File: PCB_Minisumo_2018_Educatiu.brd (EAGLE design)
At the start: 74.9 x 93 mm, 91 parts, among them Q1 BC817, Q2 BC817, Q3 BC817

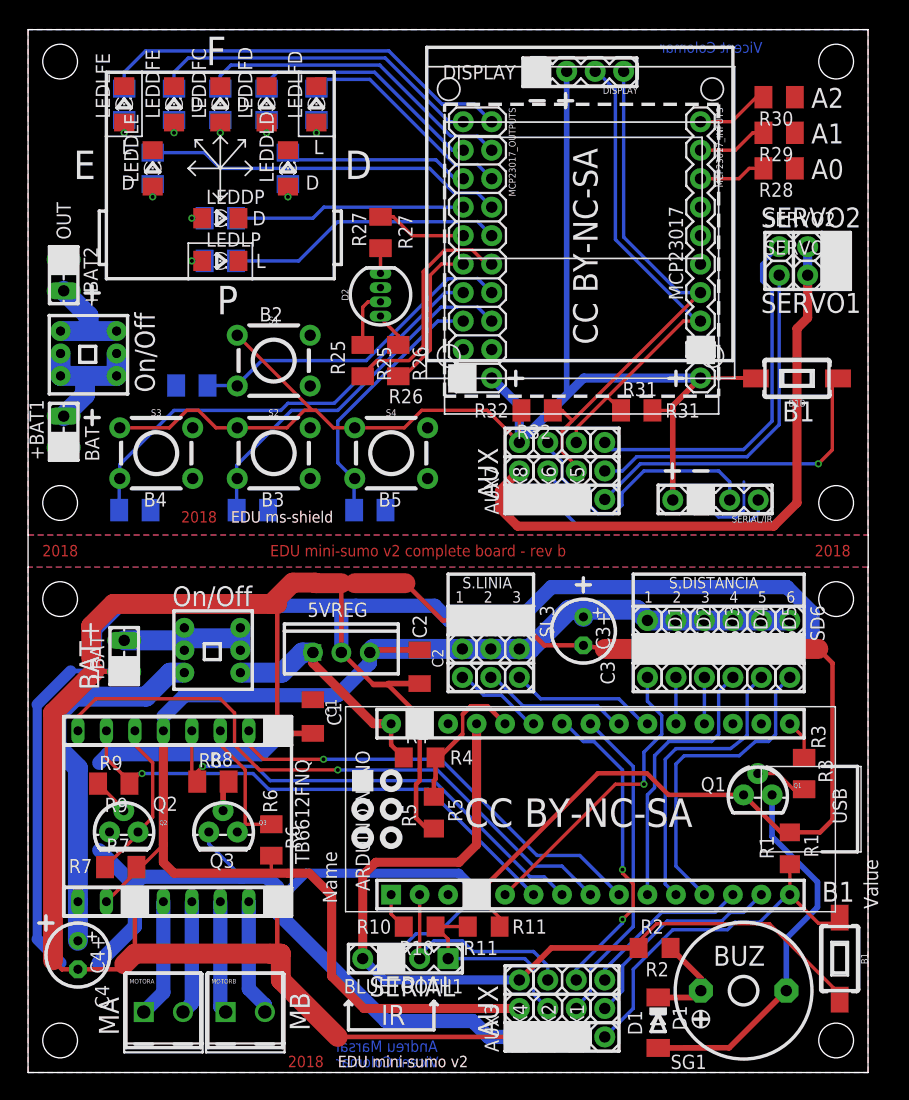
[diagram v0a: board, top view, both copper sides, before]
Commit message: Add files via upload
Corregits petits defectes en la placa.
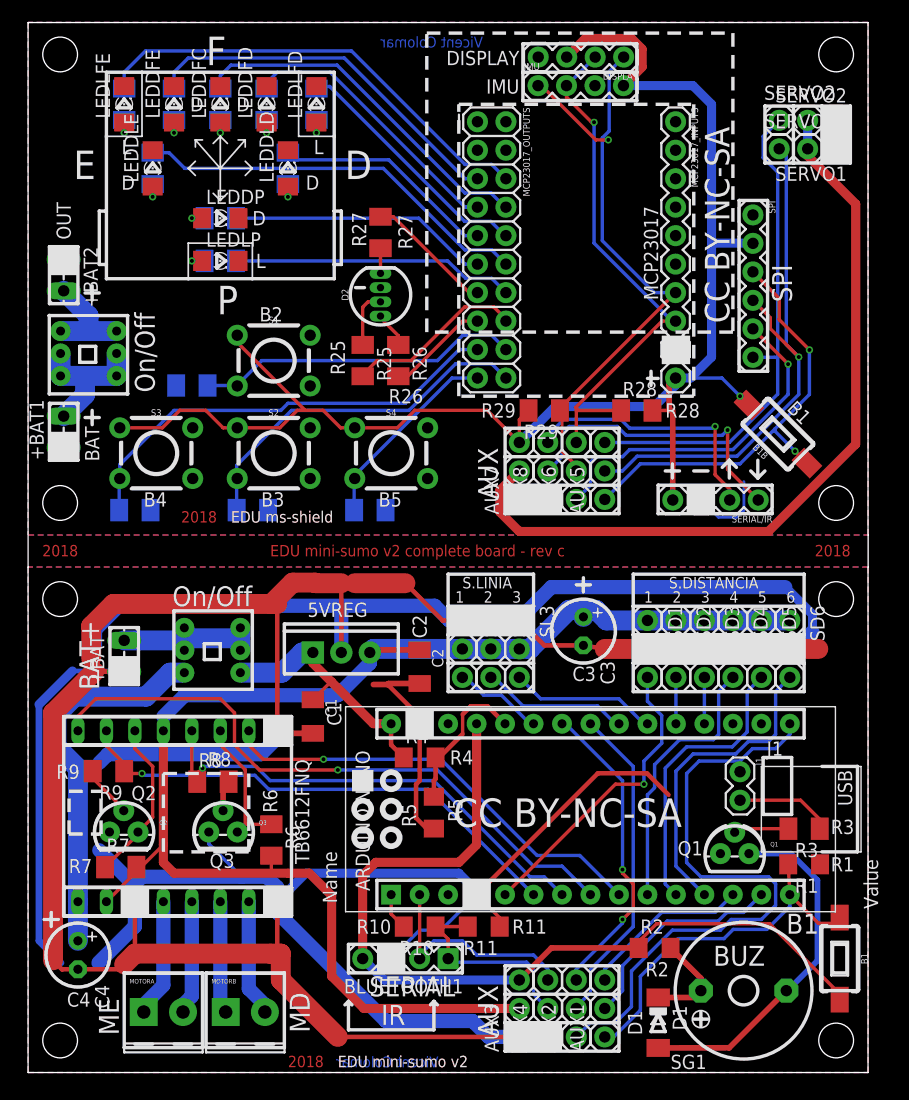
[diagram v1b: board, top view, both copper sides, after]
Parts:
- removed R30: 0R, rcl:M1206
- removed R31, R32: 4K7, rcl:M1206
- added IMU: (no value), SparkFun-Connectors:1X04
- added J1: (no value), SparkFun-Connectors:1X02
- added SPI: (no value), SparkFun-Connectors:1X06
- R28, R29: value 0R -> 4K7
- moved R29 32.4 mm to (46.0, 59.1)
- moved R28 25.0 mm to (54.3, 59.1), turned to 0 degrees
- moved SERVO2 11.3 mm to (67.0, 84.9)
- moved SERVO1 11.3 mm to (67.0, 82.4)
- moved Q1 5.63 mm to (63.0, 19.5)
- moved B1B 5.25 mm to (66.9, 56.9), turned to 135 degrees
- moved R3 4.92 mm to (69.2, 21.7), turned to 180 degrees
- moved MCP23017_INPUTS 2.22 mm to (57.8, 84.8)
- moved R1 1.91 mm to (69.2, 18.6), turned to 180 degrees
- moved DISPLAY 1.27 mm to (53.1, 90.6)
- moved MCP23017_OUTPUTS 1.27 mm to (40.1, 84.8)
- moved R9 1.21 mm to (7.17, 26.9)
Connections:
- removed net BUZZ: R3.1, U$1.D13
- new net N$1: J1.2, R3.1
- new net N$50: MCP23017_OUTPUTS.1
- new net N$51: MCP23017_OUTPUTS.2
- new net SCK_BUZZ: AUX2.1, AUX6.1, J1.1, SPI.5, U$1.D13
- net GND: now also IMU.3, SPI.1; no longer AUX2.1, AUX6.1, MCP23017_OUTPUTS.19, R28.1, R29.1, R30.1
- net MCP_A0: now also MCP23017_OUTPUTS.5, R19.2; no longer MCP23017_OUTPUTS.15, R12.2, S4.3
- net MCP_A1: now also MCP23017_OUTPUTS.7, R21.2; no longer MCP23017_OUTPUTS.13, R13.2, S3.3
- net MCP_A2: now also MCP23017_OUTPUTS.9, R23.2; no longer MCP23017_OUTPUTS.11, R26.2
- net MCP_A3: now also MCP23017_OUTPUTS.11, R24.2; no longer MCP23017_OUTPUTS.9, R27.2
- net MCP_A4: now also MCP23017_OUTPUTS.13, R27.2; no longer MCP23017_OUTPUTS.7, R24.2
- net MCP_A5: now also MCP23017_OUTPUTS.15, R26.2; no longer MCP23017_OUTPUTS.5, R23.2
- net MCP_A6: now also MCP23017_OUTPUTS.17, R13.2, S3.3; no longer MCP23017_OUTPUTS.3, R21.2
- net MCP_A7: now also MCP23017_OUTPUTS.19, R12.2, S4.3; no longer MCP23017_OUTPUTS.1, R19.2
- net MCP_B0: now also MCP23017_OUTPUTS.6, R16.2; no longer MCP23017_OUTPUTS.16, R14.2, S2.3
- net MCP_B1: now also MCP23017_OUTPUTS.8, R20.2; no longer MCP23017_OUTPUTS.14, R15.2, S1.3
- net MCP_B2: now also MCP23017_OUTPUTS.10, R18.2; no longer MCP23017_OUTPUTS.12, R25.2
- net MCP_B3: now also MCP23017_OUTPUTS.12, R22.2; no longer MCP23017_OUTPUTS.10, R17.2
- net MCP_B4: now also MCP23017_OUTPUTS.14, R17.2; no longer MCP23017_OUTPUTS.8, R22.2
- net MCP_B5: now also MCP23017_OUTPUTS.16, R25.2; no longer MCP23017_OUTPUTS.6, R18.2
- net MCP_B6: now also MCP23017_OUTPUTS.18, R15.2, S1.3; no longer MCP23017_OUTPUTS.4, R20.2
- net MCP_B7: now also MCP23017_OUTPUTS.20, R14.2, S2.3; no longer MCP23017_OUTPUTS.2, R16.2
- net MCP_DIR_A0: no longer R28.2
- net MCP_DIR_A1: no longer R29.2
- net MCP_DIR_A2: no longer R30.2
- net MCP_ITA: now also MCP23017_OUTPUTS.3; no longer MCP23017_OUTPUTS.17
- net MCP_ITB: now also MCP23017_OUTPUTS.4; no longer MCP23017_OUTPUTS.18
- net MISO: now also SPI.3
- net MOSI: now also SPI.4
- net SCL: now also IMU.2, R28.1; no longer R31.1
- net SDA: now also IMU.1, R29.1; no longer R32.1
- net SS: now also SPI.6
- net VCCARD: now also IMU.4, R28.2, R29.2, SPI.2; no longer MCP23017_OUTPUTS.20, R31.2, R32.2
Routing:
- net SCK_BUZZ: track 0.00 -> 86.8 mm, vias 0 -> 1
- net GND: track 489.3 -> 449.6 mm, vias 1 -> 0
- net MCP_A6: track 21.3 -> 40.2 mm
- net MOSI: track 50.1 -> 69.0 mm, vias 0 -> 1
- net MCP_A1: track 41.1 -> 24.7 mm
- net VCCSENS: track 186.1 -> 201.5 mm, vias 1 -> 0
- net MCP_A3: track 8.08 -> 23.2 mm
- net MCP_A7: track 30.1 -> 17.9 mm
- net SS: track 48.0 -> 60.1 mm
- net MISO: track 60.5 -> 72.3 mm, vias 1 -> 2
- net MCP_B3: track 24.8 -> 35.6 mm
- net MCP_A0: track 23.5 -> 33.5 mm
- net MCP_A4: track 20.7 -> 11.5 mm
- net N$1: track 0.00 -> 8.65 mm
- net VCCARD: track 210.5 -> 218.5 mm, vias 0 -> 1
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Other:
- board size 74.9 x 93 mm -> 74.9 x 93.7 mm
- board text added: "10/LDD"
- board text added: "11/LDP"
- board text added: "12/R"
- board text added: "13/B"
- board text added: "14/B4"
- board text added: "15/B5"
- board text added: "8/LDFE"
- board text added: "9/LDFD"
- board text added: "B1/MISO"
- board text added: "B2/6"
- board text added: "B3/7"
- board text added: "C3"
- board text added: "C4"
- board text added: "EDU mini-sumo v2 complete board - rev c"
- board text added: "G"
- board text added: "G/5"
- board text added: "GND"
- board text added: "IMU"
- board text added: "J1"
- board text added: "LDE/3"
- board text added: "LDFC/1"
- board text added: "LLFD/2"
- board text added: "LLFE/0"
- board text added: "LLP/4"
- board text added: "MD"
- board text added: "ME"
- board text added: "MISO"
- board text added: "MOSI"
- board text added: "R"
- board text added: "R28"
- board text added: "R29"
- board text added: "SCK"
- board text added: "SCK/BUZ"
- board text added: "SPI"
- board text added: "SS"
- board text added: "VCCA"
- board text added: "VCCS"
- board text removed: "0"
- board text removed: "7"
- board text removed: "A"
- board text removed: "A0"
- board text removed: "A1"
- board text removed: "A2"
- board text removed: "Andreu Marsal"
- board text removed: "C3+"
- board text removed: "C4+"
- board text removed: "D10"
- board text removed: "D11"
- board text removed: "D12"
- board text removed: "EDU mini-sumo v2 complete board - rev b"
- board text removed: "MA"
- board text removed: "MB"
- board text removed: "R31"
- board text removed: "R32"
